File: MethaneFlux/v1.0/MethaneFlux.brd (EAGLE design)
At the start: 81 x 95 mm, 59 parts, among them J1 282836-5, J2 282836-5, J3 282836-5, J4 282836-5, J5 GTFH08131YHR, P1 282837-2, U1 ADS1115IDGSR, U2 BME680, U3 74LVC125APW,118, U4 BME680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

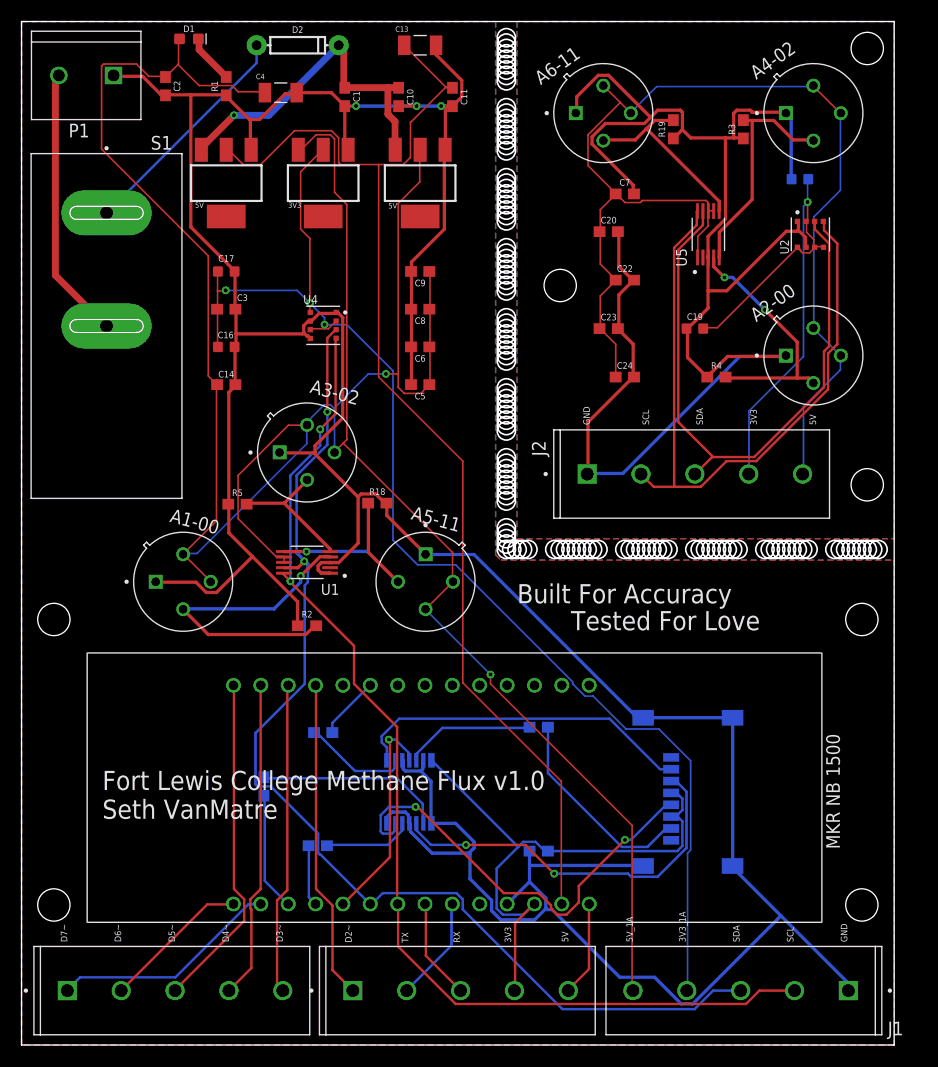
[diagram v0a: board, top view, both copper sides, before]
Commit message: Add files via upload
Added a level shifter for the BME680 for 5V I2C to 3V I2C. Added ferrite bead and 10k resistors to the ADC.
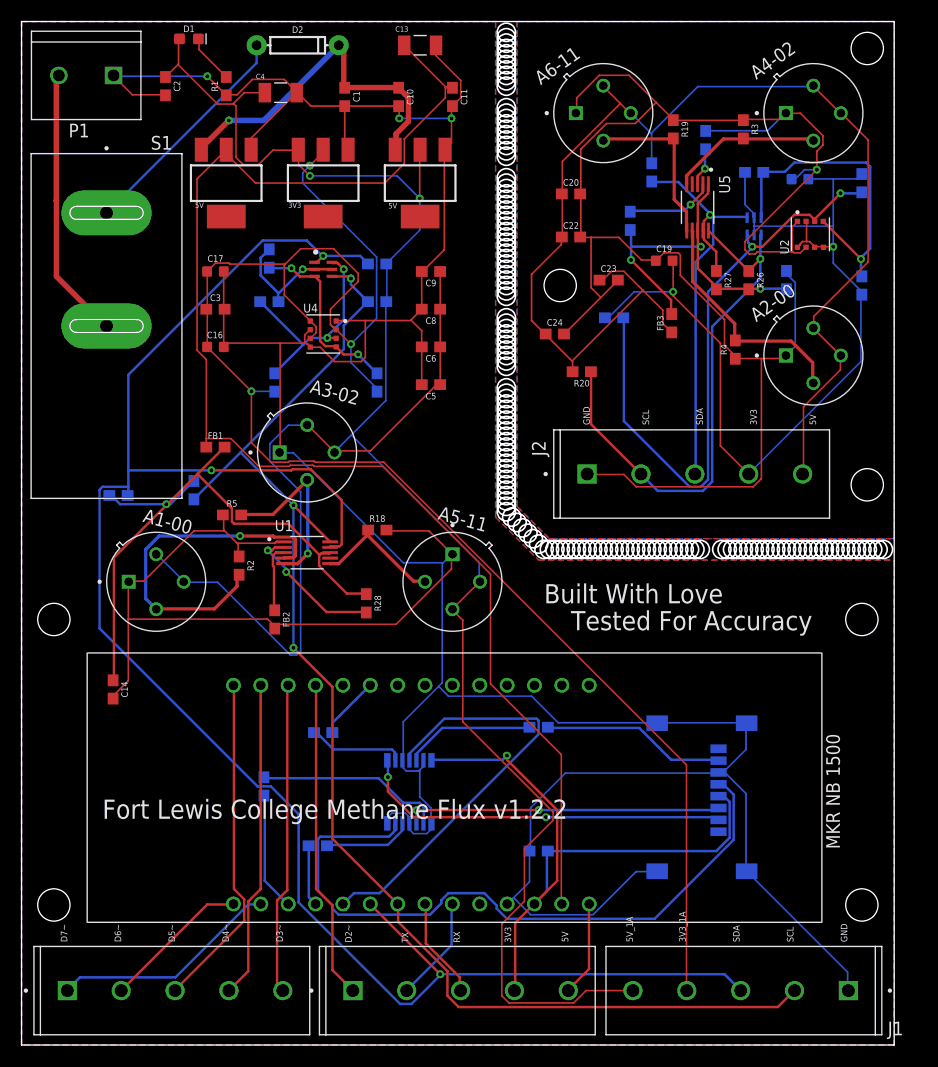
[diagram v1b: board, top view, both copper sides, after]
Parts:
- added FB1, FB2, FB3, FB4: 30Ω/1.8A, SparkFun-Coils:0603
- added R10, R11, R12, R13: 4.7k, SparkFun-Resistors:0603
- added R14, R15, R16, R17, R20, R21, R22, R23, R24, R25, R26, R27, R28, R29: 10k, SparkFun-Resistors:0603
- added U$3, U$4: 2N7002DW, 2N7002DW:SOT363
- C14, C7: value 0.1uF -> 1.0uF
- moved C14 30.2 mm to (8.50, 33.0), turned to 270 degrees
- moved C7 17.0 mm to (71.0, 71.0), flipped to the bottom, turned to 270 degrees
- moved R2 8.42 mm to (20.2, 44.5), turned to 270 degrees
- moved C24 7.63 mm to (49.5, 66.0)
- moved C19 6.91 mm to (59.6, 72.8)
- moved C22 6.40 mm to (51.0, 75.0)
- moved C20 4.95 mm to (51.0, 79.0)
- moved C23 4.50 mm to (54.5, 71.0)
- moved R4 3.09 mm to (66.2, 64.5), turned to 90 degrees
- moved U5 2.69 mm to (62.8, 77.8), turned to 270 degrees
- moved A1-00 2.50 mm to (12.5, 43.0)
- moved A5-11 2.50 mm to (40.0, 43.0)
- moved R18 2.50 mm to (33.0, 47.8)
- moved R5 1.12 mm to (19.5, 49.2)
- moved C16 1.00 mm to (18.0, 64.8)
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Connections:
- net CMD renamed DI_LLS
- net MISO renamed DO_LLS
- new net 3V3_1A: R16.2, R17.2, U$3.2, U$3.5
- new net ADC_GND: FB2.1, U1.3
- new net ADC_PWR: C14.1, FB1.2, R24.1, R25.1, R28.1, U1.8
- new net P2-SDA_3V: R10.1, R22.1, U$4.6, U2.3
- new net P2_ADC_GND: FB4.1, U5.3
- new net P2_ADC_PWR: C7.2, FB3.2, R26.2, R27.2, R29.2, U5.1, U5.8
- new net P2_SCL_3V: R11.1, R23.1, U$4.3, U2.4
- new net RDY1: R28.2, U1.2
- new net RDY2: R29.1, U5.2
- new net SCL_3V: R12.1, R17.1, U$3.3, U4.4
- new net SDA_3V: R13.1, R16.1, U$3.6, U4.3
- net 3.3V_1A: now also R12.2, R13.2
- net 3V3: no longer J5.P6
- net 5V_1A: now also R14.2, R15.2; no longer C14.2, U1.7, U1.8
- net 5V_1A_B: now also FB1.1
- net GND: now also C14.2, FB2.2, J5.P6; no longer C14.1, U1.3
- net P2-A0: now also U5.7; no longer U5.4
- net P2_3V3: now also R10.2, R11.2, R22.2, R23.2, U$4.2, U$4.5
- net P2_5V: now also FB3.1, R20.2, R21.2; no longer C7.2, U5.1, U5.7, U5.8
- net P2_GND: now also FB4.2; no longer U5.3
- net P2_SCL: now also R20.1, R26.1, U$4.4; no longer U2.4
- net P2_SDA: now also R21.1, R27.1, U$4.1; no longer U2.3
- net SCL: now also R14.1, R24.2, U$3.4; no longer U4.4
- net SDA: now also R15.1, R25.2, U$3.1; no longer U4.3
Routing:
- net SDA: track 105.5 -> 172.4 mm, vias 2 -> 3
- net ADC_PWR: track 0.00 -> 57.8 mm, vias 0 -> 1
- net P2-SDA_3V: track 0.00 -> 57.8 mm, vias 0 -> 2
- net 5V_1A: track 260.8 -> 216.7 mm
- net P2_3V3: track 49.1 -> 87.4 mm, vias 1 -> 2
- net 3.3V_1A: track 119.7 -> 154.6 mm
- net P2_ADC_PWR: track 0.00 -> 33.7 mm, vias 0 -> 3
- net P2_SCL_3V: track 0.00 -> 30.3 mm, vias 0 -> 1
- net SCK_LLS: track 40.5 -> 63.8 mm, vias 2 -> 0
- net SCL: track 102.9 -> 126.2 mm, vias 2 -> 3
- net SDA_3V: track 0.00 -> 21.2 mm, vias 0 -> 2
- net CIPO: track 20.2 -> 40.0 mm, vias 1 -> 0
- net GND: track 347.7 -> 365.9 mm
- net SCL_3V: track 0.00 -> 17.3 mm, vias 0 -> 2
- net 5V_1A_B: track 111.6 -> 127.8 mm
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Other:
- outline, holes or cut-outs redrawn
- board text added: "Built With Love"
- board text added: "Fort Lewis College Methane Flux v1.2.2"
- board text added: "Tested For Accuracy"
- board text removed: "Built For Accuracy"
- board text removed: "Fort Lewis College Methane Flux v1.0 Seth VanMatre"
- board text removed: "Tested For Love"
